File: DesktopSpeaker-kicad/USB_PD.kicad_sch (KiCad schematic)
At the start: 33 parts, among them J4 I2C service, Q1 STL9P3LLH6, Q2 STL9P3LLH6, U11 STUSB4500QTR, U18 TPS26600PWPR, U19 TPS7B8450QWDRBRQ1

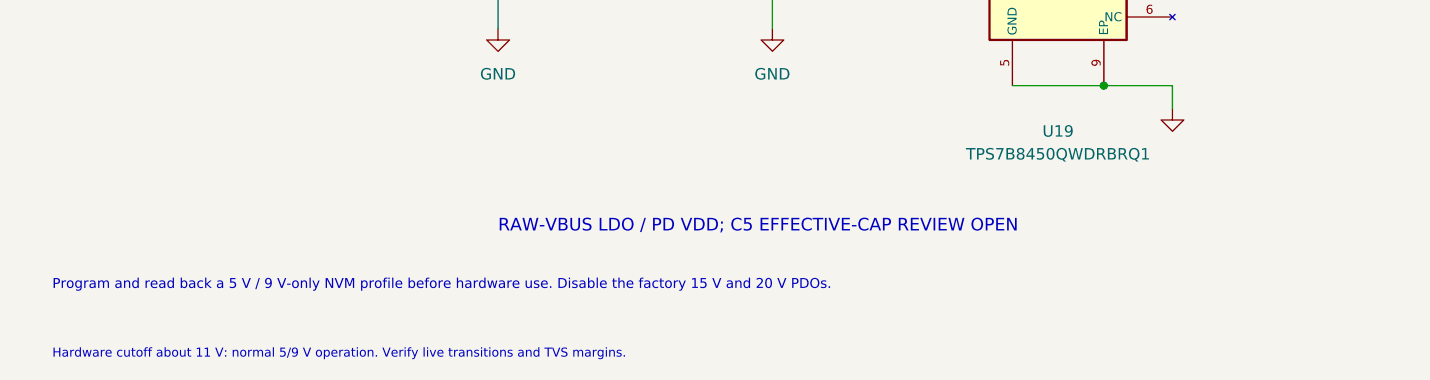
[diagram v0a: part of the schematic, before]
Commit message: Record 5-20V redesign direction and retain active hardware limits
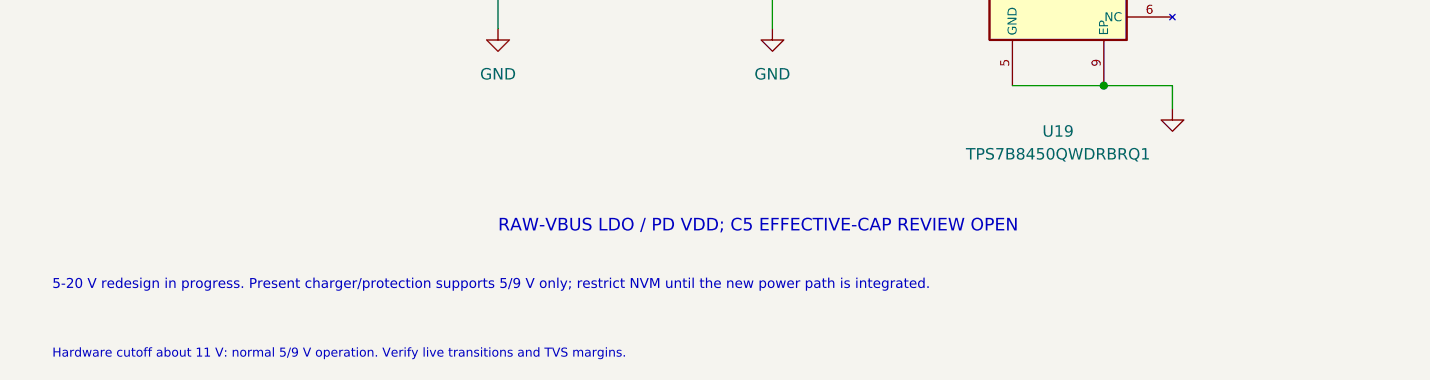
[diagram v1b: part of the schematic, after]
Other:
- note added: "5-20 V redesign in progress. Present charger/protection supports 5/9 V only; restrict NVM until the new power path is integrated."
- note removed: "Program and read back a 5 V / 9 V-only NVM profile before hardware use. Disable the factory 15 V and 20 V PDOs."
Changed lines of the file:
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@@
 (text "RAW-VBUS LDO / PD VDD; C5 EFFECTIVE-CAP REVIEW OPEN" (at 88.9 257.81 0) (effects (font (size 1.4 1.4)) (justify left bottom)))
 (text "USB-PRESENT I2C SERVICE" (at 280.67 174.625 0) (effects (font (size 1.4 1.4)) (justify left bottom)))
-(text "Program and read back a 5 V / 9 V-only NVM profile before hardware use. Disable the factory 15 V and 20 V PDOs." (at 39.37 264.16 0) (effects (font (size 1.1 1.1)) (justify left bottom)))
+(text "5-20 V redesign in progress. Present charger/protection supports 5/9 V only; restrict NVM until the new power path is integrated." (at 39.37 264.16 0) (effects (font (size 1.1 1.1)) (justify left bottom)))
 (text "J4 uses external 3.3 V logic power; disconnect the programmer when USB VBUS is absent." (at 280.67 224.79 0) (effects (font (size 1.0 1.0)) (justify left bottom)))
 (sheet_instances (path "/" (page "1")))

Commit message: Integrate USB auxiliary logic mux and reconcile active BOM
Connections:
- net PD_VDD_5V renamed USB_AUX_5V
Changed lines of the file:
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@@
 (label "DISCH" (at 115.57 177.8 0) (effects (font (size 1.0 1.0)) (justify right bottom)))
 (wire (pts (xy 171.45 157.48) (xy 181.61 157.48)) (stroke (width 0) (type default)))
-(label "PD_VDD_5V" (at 181.61 157.48 0) (effects (font (size 1.0 1.0)) (justify left bottom)))
+(label "USB_AUX_5V" (at 181.61 157.48 0) (effects (font (size 1.0 1.0)) (justify left bottom)))
 (wire (pts (xy 171.45 172.72) (xy 181.61 172.72)) (stroke (width 0) (type default)))
 (label "VBUS_VS_DISCH" (at 181.61 172.72 0) (effects (font (size 1.0 1.0)) (justify left bottom)))
@@
 (symbol (lib_id "TPS7B8450QWDRBRQ1:TPS7B8450QWDRBRQ1") (at 151.13 226.06 0) (unit 1) (exclude_from_sim no) (in_bom yes) (on_board yes) (dnp no) (instances (project "DesktopSpeaker" (path "/feda53ed-537d-4f88-9436-c6075776255b/f38b7023-3d53-43ea-b3db-e2c826d87b35" (reference "U19") (unit 1)))) (property "Reference" "U19" (at 151.13 246.38 0) (effects (font (size 1.27 1.27)))) (property "Value" "TPS7B8450QWDRBRQ1" (at 151.13 248.92 0) (effects (font (size 1.27 1.27)))) (property "Footprint" "DesktopSpeaker:TPS7B8450QWDRBRQ1_WSON-8" (at 151.13 226.06 0) (effects (font (size 1.27 1.27)) (hide yes))) (property "Datasheet" "../ai-files/datasheets/TPS7B84-Q1.pdf" (at 151.13 226.06 0) (effects (font (size 1.27 1.27)) (hide yes))) (property "Description" "Fixed 5.0 V, 150 mA automotive LDO, WSON-8 DRB with exposed thermal pad" (at 151.13 226.06 0) (effects (font (size 1.27 1.27)) (hide yes))) (property "Manufacturer" "Texas Instruments" (at 151.13 226.06 0) (effects (font (size 1.27 1.27)) (hide yes))) (property "MPN" "TPS7B8450QWDRBRQ1" (at 151.13 226.06 0) (effects (font (size 1.27 1.27)) (hide yes))) (pin "8") (pin "7") (pin "1") (pin "2") (pin "3") (pin "4") (pin "6") (pin "5") (pin "9") (property "LCSC Part" "C3751394" (at 151.13 226.06 0) (effects (font (size 1.27 1.27)) (hide yes))))
 (symbol (lib_id "power:GND") (at 163.83 243.84 0) (unit 1) (exclude_from_sim no) (in_bom no) (on_board no) (dnp no) (property "Reference" "#PWR191" (at 163.83 247.65 0) (effects (font (size 1.27 1.27)) (hide yes))) (property "Value" "GND" (at 163.83 248.92000000000002 0) (effects (font (size 1.27 1.27)) (hide yes))) (pin "1") (instances (project "DesktopSpeaker" (path "/feda53ed-537d-4f88-9436-c6075776255b/f38b7023-3d53-43ea-b3db-e2c826d87b35" (reference "#PWR191") (unit 1)))))
-(label "PD_VDD_5V" (at 199.39 218.44 0) (effects (font (size 1 1)) (justify left bottom)))
 (wire (pts (xy 88.9 222.25) (xy 88.9 215.9)) (stroke (width 0) (type default)))
 (wire (pts (xy 88.9 215.9) (xy 119.38 215.9)) (stroke (width 0) (type default)))
@@
 (junction (at 119.38 215.9) (diameter 0) (color 0 0 0 0))
 (junction (at 135.89 220.98) (diameter 0) (color 0 0 0 0))
-(junction (at 156.21 241.3) (diameter 0) (color 0 0 0 0)))
+(junction (at 156.21 241.3) (diameter 0) (color 0 0 0 0))
+(wire (pts (xy 199.39 218.44) (xy 226.06 218.44)) (stroke (width 0) (type default)))
+(junction (at 199.39 218.44) (diameter 0) (color 0 0 0 0))
+(hierarchical_label "USB_AUX_5V" (shape output) (at 226.06 218.44 0) (effects (font (size 1 1)) (justify left bottom))))
